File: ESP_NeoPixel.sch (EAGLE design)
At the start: 19 parts, among them J1 CONN_08, J2 CONN_08, J3 MKDS3-2-5.00, J4 MKDS3-3-5.00, Q1 BSN20,215, U1 LMZ21700

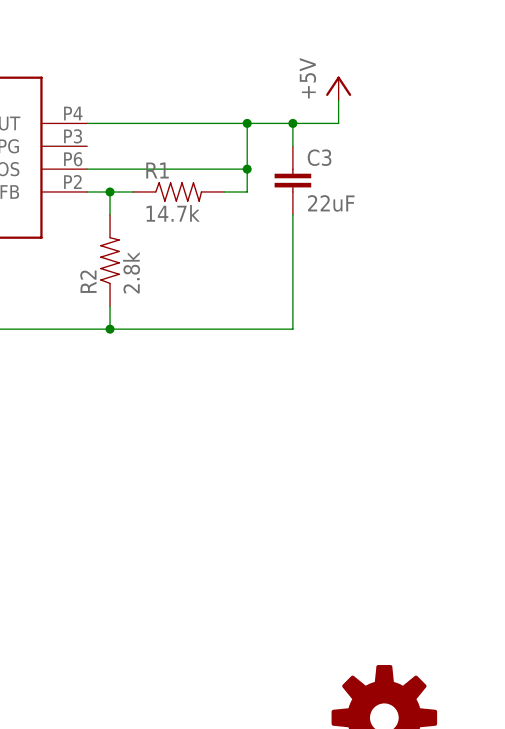
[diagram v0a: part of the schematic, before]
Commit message: added switch to D8
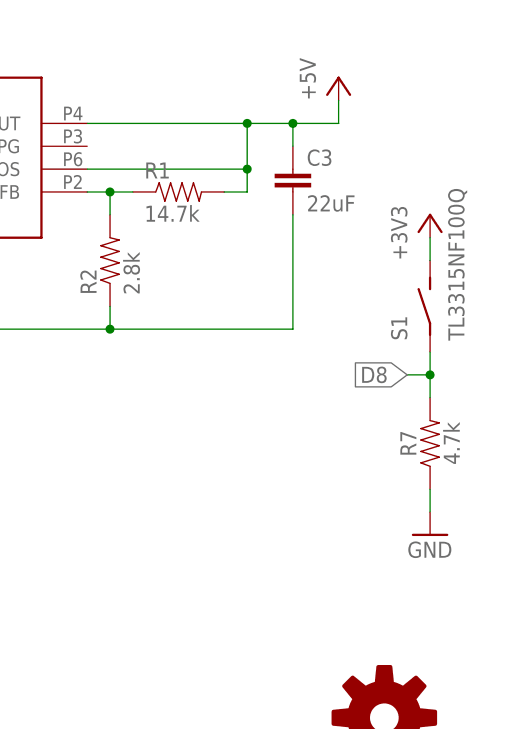
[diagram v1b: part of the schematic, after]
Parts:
- added R7: 4.7k, SparkFun-Resistors:RESISTOR0603
- added S1: TL3315NF100Q, jonas-switch:TL3315NF100Q
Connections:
- net +3V3: now also S1.S
- net D8: now also R7.2, S1.P
- net GND: now also R7.1
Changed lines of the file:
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@@
 <part name="GND6" library="supply1" library_urn="urn:adsk.eagle:library:371" deviceset="GND" device=""/>
 <part name="R6" library="SparkFun-Resistors" library_urn="urn:adsk.eagle:library:532" deviceset="RESISTOR" device="0603" package3d_urn="urn:adsk.eagle:package:39650/1" value=" "/>
+<part name="S1" library="jonas-switch" deviceset="TL3315NF100Q" device=""/>
+<part name="R7" library="SparkFun-Resistors" library_urn="urn:adsk.eagle:library:532" deviceset="RESISTOR" device="0603" package3d_urn="urn:adsk.eagle:package:39650/1" value="4.7k"/>
+<part name="+3V2" library="supply1" library_urn="urn:adsk.eagle:library:371" deviceset="+3V3" device=""/>
+<part name="GND7" library="supply1" library_urn="urn:adsk.eagle:library:371" deviceset="GND" device=""/>
 </parts>
 <sheets>
@@
 <attribute name="NAME" x="44.2214" y="148.59" size="1.778" layer="95" rot="R90"/>
 </instance>
+<instance part="S1" gate="G$1" x="218.44" y="124.46">
+<attribute name="NAME" x="215.9" y="120.65" size="1.778" layer="95" rot="R90"/>
+<attribute name="VALUE" x="222.25" y="120.65" size="1.778" layer="96" rot="R90"/>
+</instance>
+<instance part="R7" gate="G$1" x="218.44" y="109.22" rot="R90">
+<attribute name="NAME" x="216.916" y="109.22" size="1.778" layer="95" font="vector" rot="R90" align="bottom-center"/>
+<attribute name="VALUE" x="219.964" y="109.22" size="1.778" layer="96" font="vector" rot="R90" align="top-center"/>
+</instance>
+<instance part="+3V2" gate="G$1" x="218.44" y="134.62">
+<attribute name="VALUE" x="215.9" y="129.54" size="1.778" layer="96" rot="R90"/>
+</instance>
+<instance part="GND7" gate="1" x="218.44" y="99.06">
+<attribute name="VALUE" x="215.9" y="96.52" size="1.778" layer="96"/>
+</instance>
 </instances>
 <busses>
@@
 <wire x1="45.72" y1="30.48" x2="33.02" y2="30.48" width="0.1524" layer="91"/>
 <label x="35.56" y="30.48" size="1.778" layer="95"/>
+</segment>
+<segment>
+<pinref part="S1" gate="G$1" pin="P"/>
+<pinref part="R7" gate="G$1" pin="2"/>
+<wire x1="218.44" y1="119.38" x2="218.44" y2="116.84" width="0.1524" layer="91"/>
+<wire x1="218.44" y1="116.84" x2="218.44" y2="114.3" width="0.1524" layer="91"/>
+<wire x1="218.44" y1="116.84" x2="215.9" y2="116.84" width="0.1524" layer="91"/>
+<junction x="218.44" y="116.84"/>
+<label x="215.9" y="116.84" size="1.778" layer="95" rot="R180" xref="yes"/>
 </segment>
 </net>
@@
 <wire x1="45.72" y1="134.62" x2="45.72" y2="137.16" width="0.1524" layer="91"/>
 </segment>
+<segment>
+<pinref part="R7" gate="G$1" pin="1"/>
+<pinref part="GND7" gate="1" pin="GND"/>
+<wire x1="218.44" y1="104.14" x2="218.44" y2="101.6" width="0.1524" layer="91"/>
+</segment>
 </net>
 <net name="+3V3" class="0">
@@
 <pinref part="+3V5" gate="G$1" pin="+3V3"/>
 </segment>
-</net>
+<segment>
+<pinref part="+3V2" gate="G$1" pin="+3V3"/>
+<pinref part="S1" gate="G$1" pin="S"/>
+<wire x1="218.44" y1="132.08" x2="218.44" y2="129.54" width="0.1524" layer="91"/>
+</segment>
+</net>
